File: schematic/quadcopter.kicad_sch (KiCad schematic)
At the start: 1 part, among them U1 RaspberryPi_4B

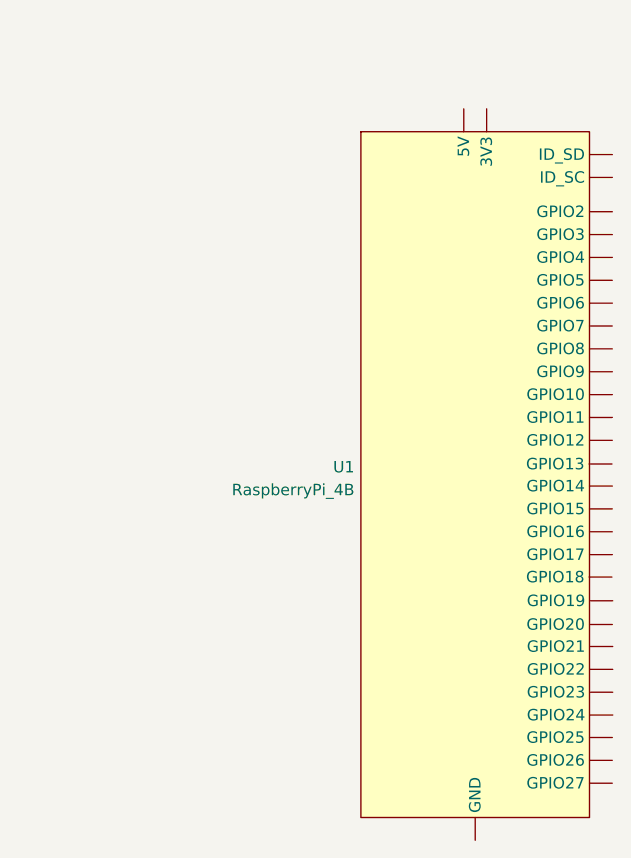
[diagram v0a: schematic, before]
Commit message: Use RPi symbol/footprint from SnapEDA
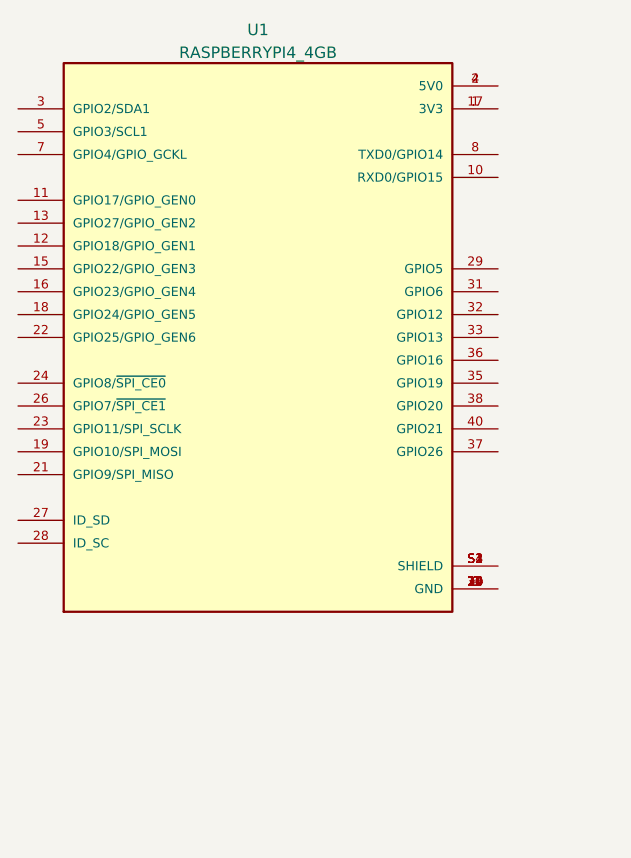
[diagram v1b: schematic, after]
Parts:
- removed U1: RaspberryPi_4B, symbol quadcopter:RaspberryPi_4B
- added U1: RASPBERRYPI4_4GB, MODULE_RASPBERRYPI4_4GB, symbol RASPBERRYPI4_4GB:RASPBERRYPI4_4GB
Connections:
- new net: U1.1 (3V3), U1.17 (3V3)
- new net: U1.14 (GND), U1.20 (GND), U1.25 (GND), U1.30 (GND), U1.34 (GND), U1.39 (GND), U1.6 (GND), U1.9 (GND)
- new net: U1.2 (5V0), U1.4 (5V0)
- new net: U1.S1 (SHIELD), U1.S2 (SHIELD), U1.S3 (SHIELD), U1.S4 (SHIELD)
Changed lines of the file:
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@@
     (title "Quadcopter")
   )
-  (symbol (lib_id "quadcopter:RaspberryPi_4B") (at 107.95 104.14 0) (unit 1)
+  (symbol (lib_id "RASPBERRYPI4_4GB:RASPBERRYPI4_4GB") (at 85.09 83.82 0) (unit 1)
     (in_bom yes) (on_board yes) (fields_autoplaced)
-    (property "Reference" "U1" (id 0) (at 94.5389 103.3053 0)
-      (effects (font (size 1.27 1.27)) (justify right))
+    (property "Reference" "U1" (id 0) (at 83.82 54.7202 0))
+    (property "Value" "RASPBERRYPI4_4GB" (id 1) (at 83.82 57.2571 0))
+    (property "Footprint" "MODULE_RASPBERRYPI4_4GB" (id 2) (at 85.09 83.82 0)
+      (effects (font (size 1.27 1.27)) (justify left bottom) hide)
     )
-    (property "Value" "RaspberryPi_4B" (id 1) (at 94.5389 105.8422 0)
-      (effects (font (size 1.27 1.27)) (justify right))
+    (property "Datasheet" "" (id 3) (at 85.09 83.82 0)
+      (effects (font (size 1.27 1.27)) (justify left bottom) hide)
     )
-    (property "Footprint" "" (id 2) (at 107.95 91.44 0)
-      (effects (font (size 1.27 1.27)) hide)
+    (property "MANUFACTURER" "Raspberry Pi" (id 4) (at 85.09 83.82 0)
+      (effects (font (size 1.27 1.27)) (justify left bottom) hide)
     )
-    (property "Datasheet" "" (id 3) (at 107.95 91.44 0)
-      (effects (font (size 1.27 1.27)) hide)
+    (property "MAXIMUM_PACKAGE_HIEGHT" "18mm" (id 5) (at 85.09 83.82 0)
+      (effects (font (size 1.27 1.27)) (justify left bottom) hide)
     )
-    (pin "")
-    (pin "")
-    (pin "")
-    (pin "")
-    (pin "")
-    (pin "")
-    (pin "")
-    (pin "")
-    (pin "")
-    (pin "")
-    (pin "")
-    (pin "")
-    (pin "")
-    (pin "")
-    (pin "")
-    (pin "")
-    (pin "")
-    (pin "")
-    (pin "")
-    (pin "")
-    (pin "")
-    (pin "")
-    (pin "")
-    (pin "")
-    (pin "")
-    (pin "")
-    (pin "")
-    (pin "")
-    (pin "")
-    (pin "")
-    (pin "")
+    (property "STANDARD" "Manufacturer Recommendations" (id 6) (at 85.09 83.82 0)
+      (effects (font (size 1.27 1.27)) (justify left bottom) hide)
+    )
+    (property "PARTREV" "1.0" (id 7) (at 85.09 83.82 0)
+      (effects (font (size 1.27 1.27)) (justify left bottom) hide)
+    )
+    (pin "1")
+    (pin "10")
+    (pin "11")
+    (pin "12")
+    (pin "13")
+    (pin "14")
+    (pin "15")
+    (pin "16")
+    (pin "17")
+    (pin "18")
+    (pin "19")
+    (pin "2")
+    (pin "20")
+    (pin "21")
+    (pin "22")
+    (pin "23")
+    (pin "24")
+    (pin "25")
+    (pin "26")
+    (pin "27")
+    (pin "28")
+    (pin "29")
+    (pin "3")
+    (pin "30")
+    (pin "31")
+    (pin "32")
+    (pin "33")
+    (pin "34")
+    (pin "35")
+    (pin "36")
+    (pin "37")
+    (pin "38")
+    (pin "39")
+    (pin "4")
+    (pin "40")
+    (pin "5")
+    (pin "6")
+    (pin "7")
+    (pin "8")
+    (pin "9")
+    (pin "S1")
+    (pin "S2")
+    (pin "S3")
+    (pin "S4")
   )
   (sheet_instances
@@
   )
   (symbol_instances
-    (path "/10f7aa14-ce94-484c-ac6b-3b47fa9d072d"
-      (reference "U1") (unit 1) (value "RaspberryPi_4B") (footprint "")
+    (path "/68bb99c0-3e71-424d-a793-4153ce8977e1"
+      (reference "U1") (unit 1) (value "RASPBERRYPI4_4GB") (footprint "MODULE_RASPBERRYPI4_4GB")
     )
   )
